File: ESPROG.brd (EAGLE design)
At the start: 30 x 20 mm, 20 parts, among them IC1 CP2104, J1 USB-C, J2 M06RA, Q3 MMDT3904

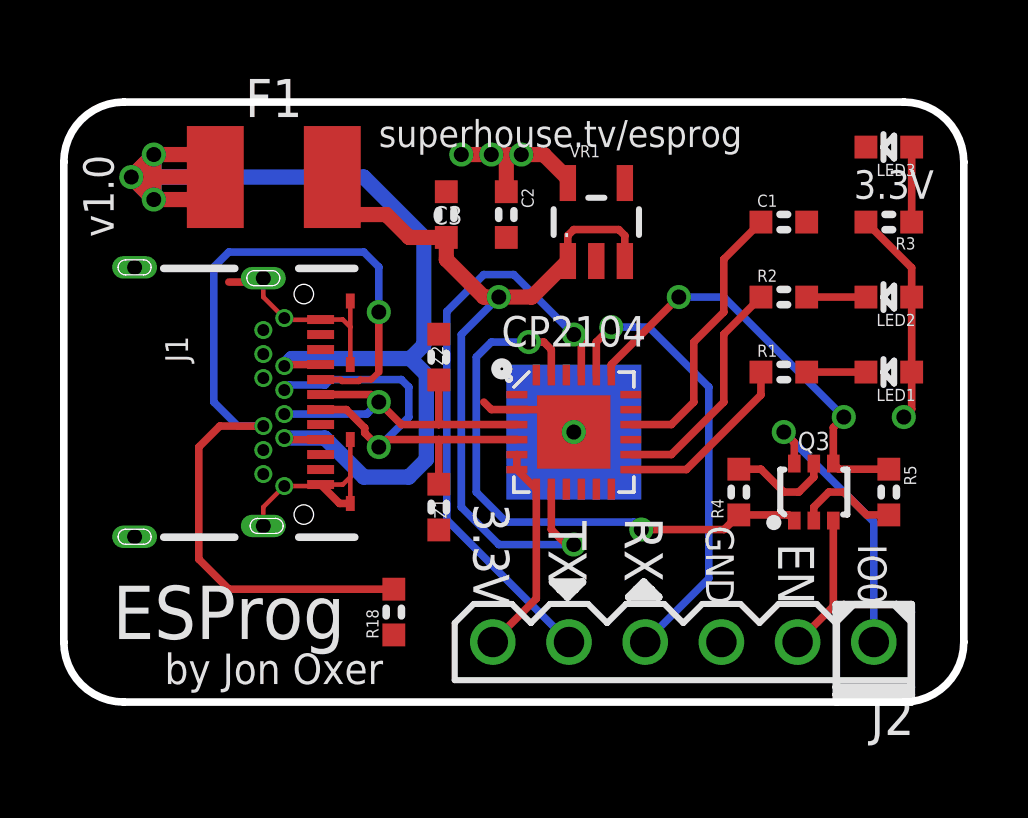
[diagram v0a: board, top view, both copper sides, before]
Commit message: Renumbered parts
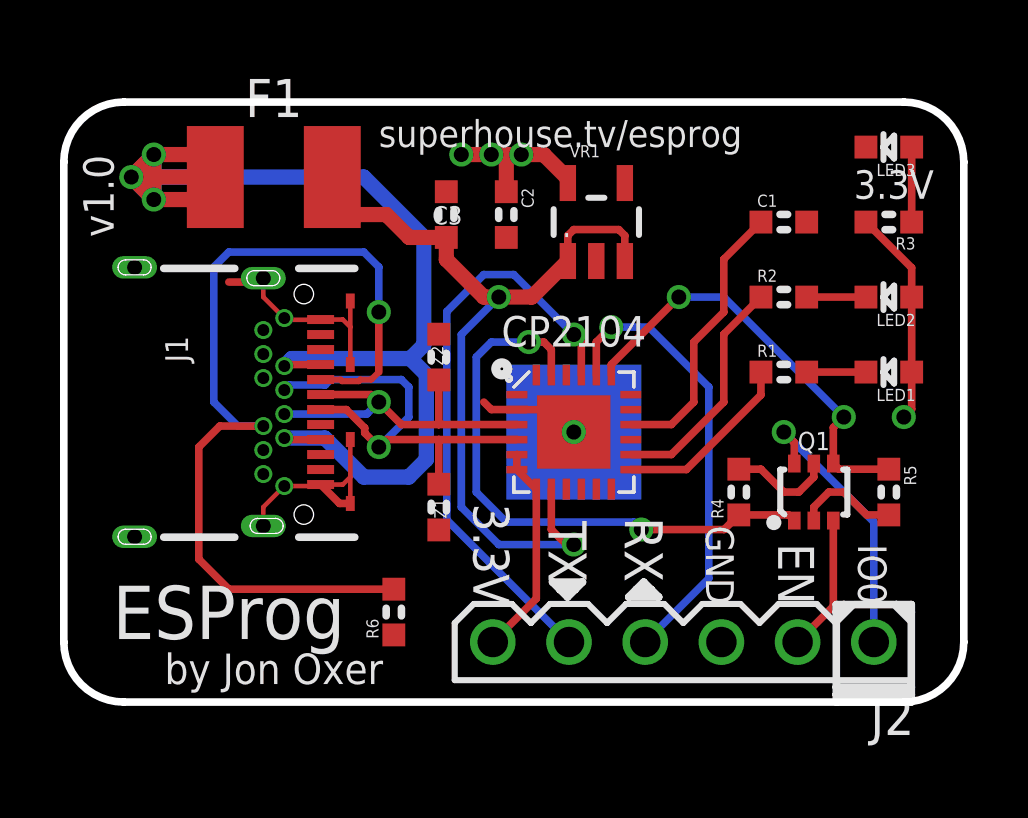
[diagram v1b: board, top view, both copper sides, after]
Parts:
- renumbered Q3 to Q1, R18 to R6
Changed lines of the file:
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@@
 <drawing>
 <settings>
-<setting alwaysvectorfont="yes"/>
+<setting alwaysvectorfont="no"/>
 <setting keepoldvectorfont="yes"/>
 <setting verticaltext="up"/>
@@
 <attribute name="VALUE" x="2.155" y="11.605" size="0.762" layer="27" rot="R270"/>
 </element>
-<element name="R18" library="SuperHouse-DiscreteSemi" library_urn="urn:adsk.eagle:library:11768461" package="R0603" package3d_urn="urn:adsk.eagle:package:11768543/2" value="5.1K" x="11" y="3" smashed="yes" rot="R90">
+<element name="R6" library="SuperHouse-DiscreteSemi" library_urn="urn:adsk.eagle:library:11768461" package="R0603" package3d_urn="urn:adsk.eagle:package:11768543/2" value="5.1K" x="11" y="3" smashed="yes" rot="R90">
 <attribute name="NAME" x="10.492" y="2.111" size="0.4064" layer="25" font="vector" rot="R90"/>
 <attribute name="VALUE" x="10.4652" y="1.884" size="0.8128" layer="27" font="vector" rot="R90"/>
@@
 <attribute name="VALUE" x="26.5348" y="8.016" size="0.4064" layer="27" font="vector" rot="R270"/>
 </element>
-<element name="Q3" library="SuperHouse-DiscreteSemi" library_urn="urn:adsk.eagle:library:11768461" package="SOT-363" package3d_urn="urn:adsk.eagle:package:11799616/2" value="MMDT3904" x="25" y="7" smashed="yes">
+<element name="Q1" library="SuperHouse-DiscreteSemi" library_urn="urn:adsk.eagle:library:11768461" package="SOT-363" package3d_urn="urn:adsk.eagle:package:11799616/2" value="MMDT3904" x="25" y="7" smashed="yes">
 <attribute name="NAME" x="25" y="8.397" size="0.6096" layer="25" font="vector" ratio="16" align="bottom-center"/>
 <attribute name="PROD_ID" value="TRANS-13337" x="25" y="7" size="1.778" layer="27" display="off"/>
@@
 <contactref element="J1" pad="CASE3"/>
 <contactref element="J1" pad="CASE4"/>
-<contactref element="R18" pad="1"/>
+<contactref element="R6" pad="1"/>
 <wire x1="8.56" y1="7.25" x2="9.19" y2="6.62" width="0.254" layer="1"/>
 <wire x1="9.19" y1="6.62" x2="9.55" y2="6.62" width="0.254" layer="1"/>
@@
 <contactref element="J1" pad="A5"/>
 <contactref element="J1" pad="B5"/>
-<contactref element="R18" pad="2"/>
+<contactref element="R6" pad="2"/>
 <wire x1="6.65" y1="9.2" x2="5.2" y2="9.2" width="0.254" layer="1"/>
 <via x="10.5" y="13" extent="1-16" drill="0.5"/>
@@
 <signal name="EN">
 <contactref element="J2" pad="2"/>
-<contactref element="Q3" pad="3"/>
+<contactref element="Q1" pad="3"/>
 <wire x1="25.65" y1="6.05" x2="25.65" y2="3.19" width="0.254" layer="1"/>
 <wire x1="25.65" y1="3.19" x2="24.46" y2="2" width="0.254" layer="1"/>
@@
 <signal name="GPIO0">
 <contactref element="J2" pad="1"/>
-<contactref element="Q3" pad="6"/>
+<contactref element="Q1" pad="6"/>
 <wire x1="24.35" y1="7.95" x2="24.35" y2="8.65" width="0.254" layer="1"/>
 <wire x1="24.35" y1="8.65" x2="24" y2="9" width="0.254" layer="1"/>
@@
 </signal>
 <signal name="N$7">
-<contactref element="Q3" pad="5"/>
+<contactref element="Q1" pad="5"/>
 <contactref element="R4" pad="2"/>
 <wire x1="22.5" y1="7.762" x2="23.238" y2="7.762" width="0.254" layer="1"/>
@@
 </signal>
 <signal name="N$8">
-<contactref element="Q3" pad="2"/>
+<contactref element="Q1" pad="2"/>
 <contactref element="R5" pad="2"/>
 <wire x1="27.5" y1="6.238" x2="26.762" y2="6.238" width="0.254" layer="1"/>
@@
 <signal name="DTR">
 <contactref element="R4" pad="1"/>
-<contactref element="Q3" pad="1"/>
+<contactref element="Q1" pad="1"/>
 <contactref element="IC1" pad="23"/>
 <wire x1="22.5" y1="6.238" x2="24.162" y2="6.238" width="0.254" layer="1"/>
@@
 <signal name="RTS">
 <contactref element="R5" pad="1"/>
-<contactref element="Q3" pad="4"/>
+<contactref element="Q1" pad="4"/>
 <contactref element="IC1" pad="19"/>
 <wire x1="27.5" y1="7.762" x2="25.838" y2="7.762" width="0.254" layer="1"/>
